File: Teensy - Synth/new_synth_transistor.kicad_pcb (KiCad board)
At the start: 2 copper layers, 88 parts, among them J1 Conn_01x07_Male, J2 Conn_01x07_Male, J3 Conn_01x07_Male, J4 Conn_01x07_Male, J5 USB_B, J6 Conn_ARM_JTAG_SWD_10, J7 USB_B, J8 Conn_01x02_Male, Q1 MMBT3904, Q2 MMBT3904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

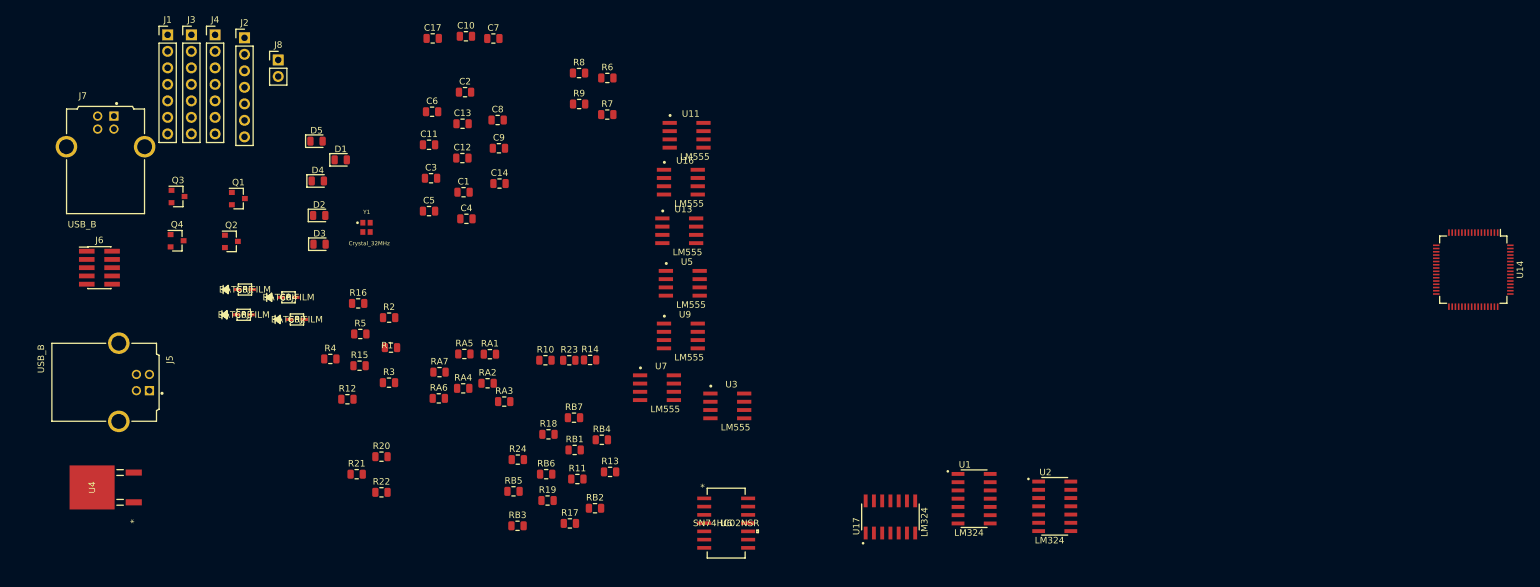
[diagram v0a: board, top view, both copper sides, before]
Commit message: Revert to Teesy PCB files
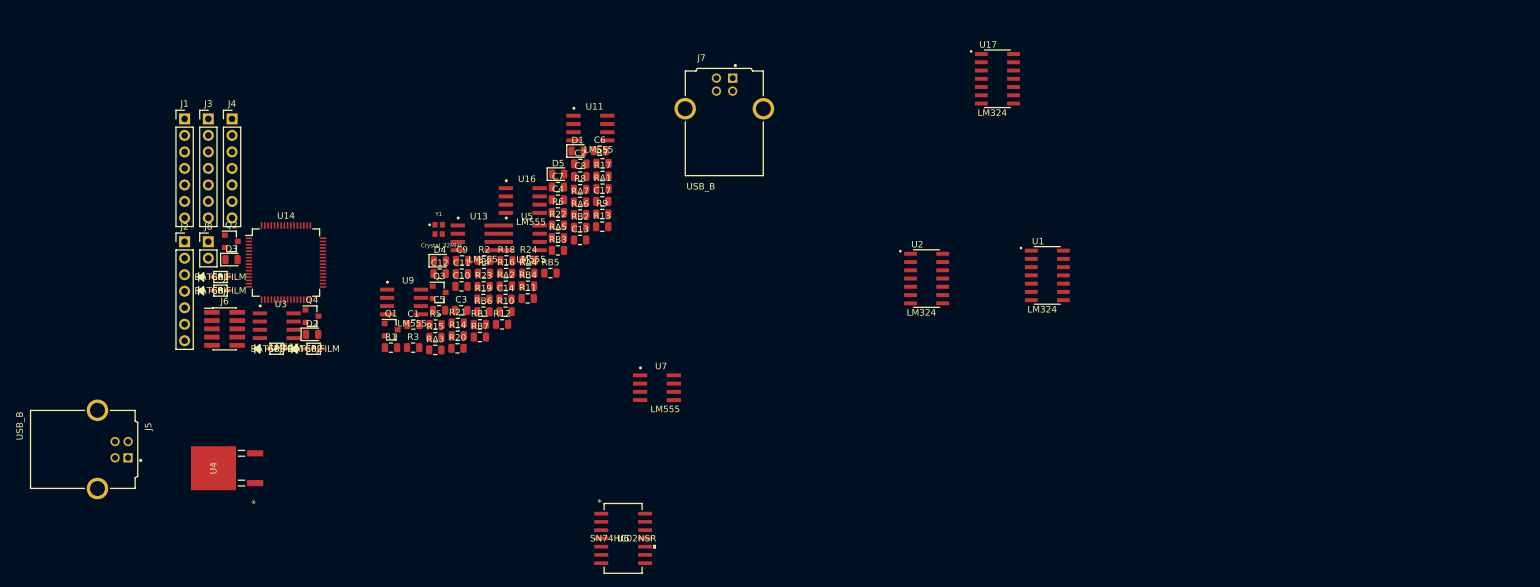
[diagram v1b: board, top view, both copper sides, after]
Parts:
- moved U14 182.7 mm to (49.8, 49.3), turned to 0 degrees
- moved J7 95.4 mm to (117.2, 27.7)
- moved U3 70.4 mm to (48.3, 59.0)
- moved U17 69.4 mm to (159.2, 21.0), turned to 0 degrees
- moved R17 53.7 mm to (98.5, 36.0)
- moved R22 49.3 mm to (91.6, 43.5)
- moved RB2 43.3 mm to (95.0, 43.8)
- moved U9 42.9 mm to (67.9, 55.3)
- moved RB3 42.8 mm to (91.6, 47.4)
- moved Q3 42.8 mm to (73.3, 53.9)
- moved U2 40.2 mm to (148.3, 51.7)
- moved C10 38.5 mm to (76.8, 52.9)
- moved R13 37.8 mm to (98.4, 43.8)
- moved D5 37.5 mm to (91.6, 35.7)
- moved D1 36.5 mm to (94.6, 32.1)
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
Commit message: do not pull, trying to fix kicad libraries
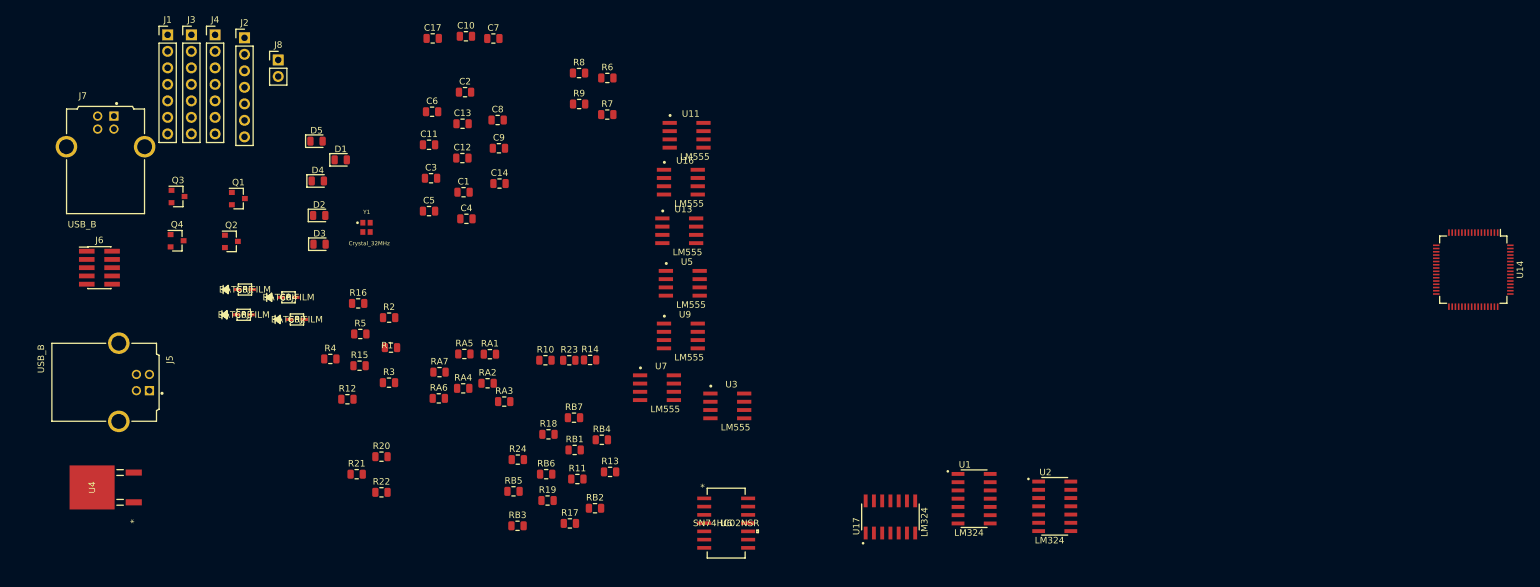
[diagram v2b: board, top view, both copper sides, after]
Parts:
- moved U14 182.7 mm to (232.5, 50.4), turned to 270 degrees
- moved J7 95.4 mm to (22.0, 33.5)
- moved U3 70.4 mm to (117.7, 71.3)
- moved U17 69.4 mm to (142.8, 88.4), turned to 90 degrees
- moved R17 53.7 mm to (93.4, 89.4)
- moved R22 49.3 mm to (64.4, 84.6)
- moved RB2 43.3 mm to (97.3, 87.1)
- moved U9 42.9 mm to (110.5, 60.6)
- moved RB3 42.8 mm to (85.4, 89.8)
- moved Q3 42.8 mm to (33.1, 39.1)
- moved U2 40.2 mm to (168.1, 86.8)
- moved C10 38.5 mm to (77.4, 14.5)
- moved R13 37.8 mm to (99.6, 81.5)
- moved D5 37.5 mm to (54.5, 30.6)
- moved D1 36.5 mm to (58.2, 33.5)
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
